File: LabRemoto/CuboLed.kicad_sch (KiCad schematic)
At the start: 42 parts

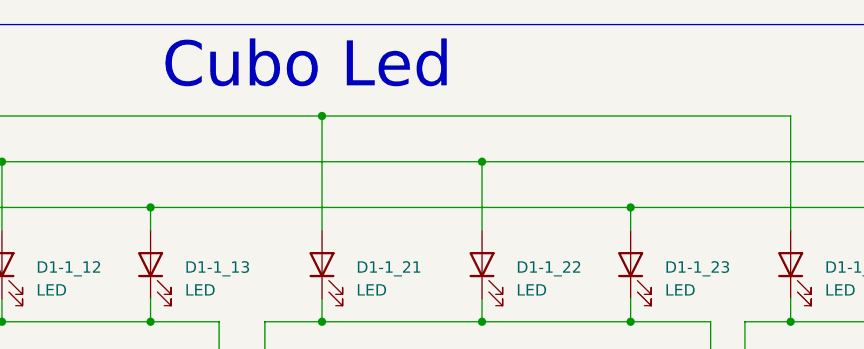
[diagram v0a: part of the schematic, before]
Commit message: Se corrigieron esquemas
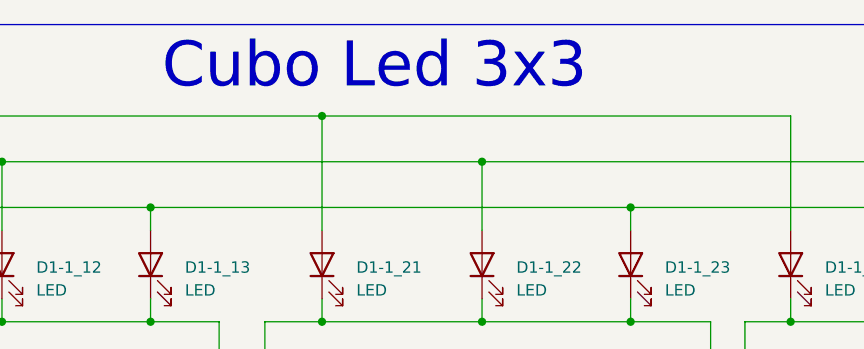
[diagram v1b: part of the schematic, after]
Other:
- note added: "Cubo Led 3x3"
- note removed: "Cubo Led"
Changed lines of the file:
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@@
     (stroke (width 0) (type default))
   )
-  (text "Cubo Led" (at 124.46 27.94 0)
+  (text "Cubo Led 3x3\n" (at 124.46 27.94 0)
     (effects (font (size 5 5)) (justify left bottom))
   )
